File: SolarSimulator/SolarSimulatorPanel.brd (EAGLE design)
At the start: 155 x 77 mm, 82 parts, among them U1 Red Driver, U2 Green Driver, U3 Blue Driver, X1 MKDSN1,5/2-5,08

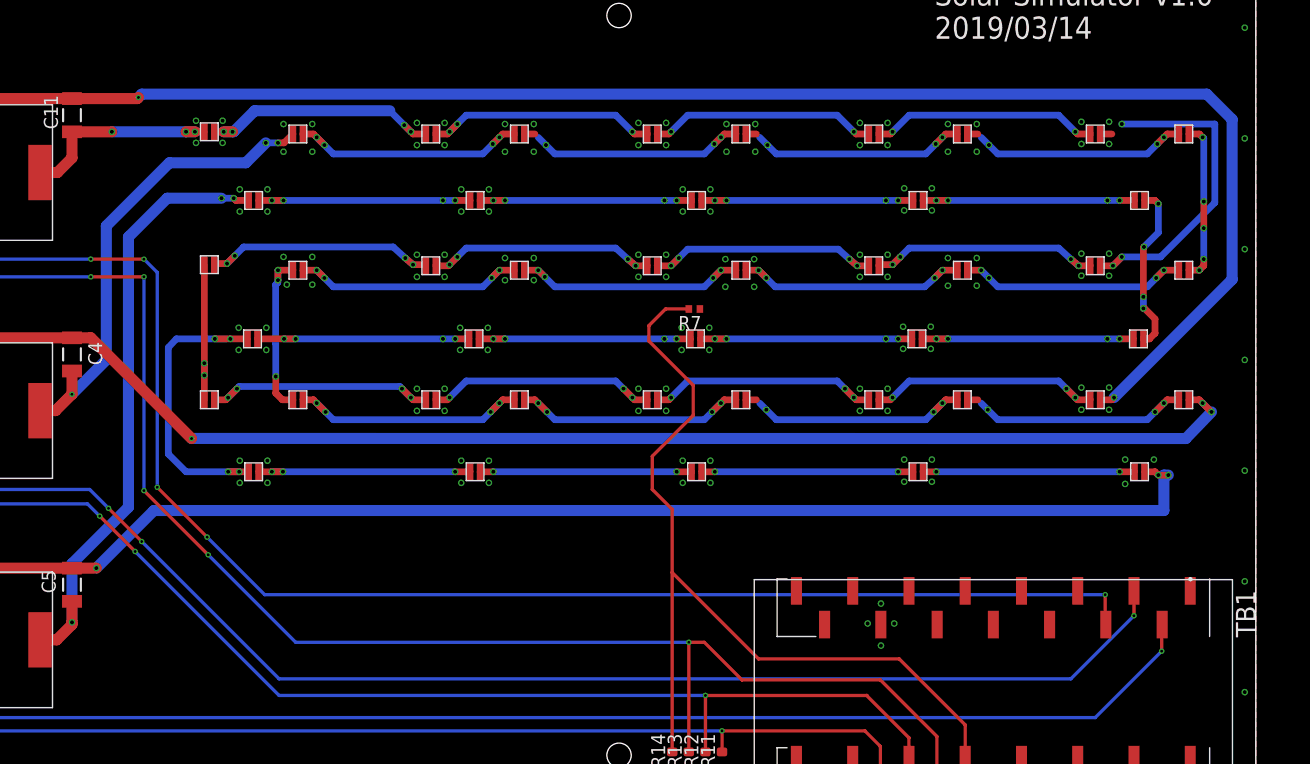
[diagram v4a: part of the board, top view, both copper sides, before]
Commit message: Copper cleanup of solar simulator board. Left LEDs about where they were as much as possible, moved origins ot center on LEDs, tried to sink as much heat to the bottom layer as possible.
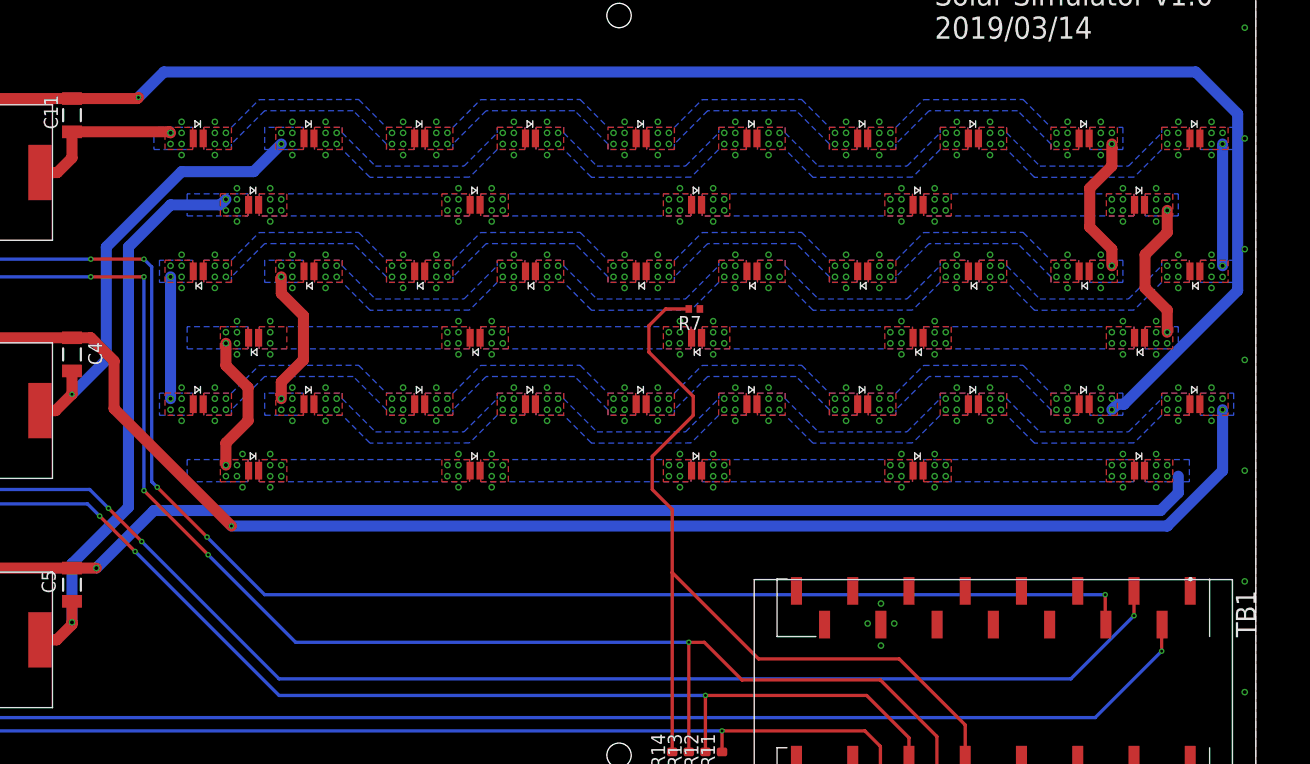
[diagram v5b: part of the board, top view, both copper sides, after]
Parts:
- moved BLUE10 2.28 mm to (59.5, 49.0)
- moved BLUE6 2.22 mm to (139.5, 49.0)
- moved BLUE7 2.22 mm to (119.5, 49.0)
- moved BLUE8 2.22 mm to (99.5, 49.0)
- moved BLUE9 2.22 mm to (79.5, 49.0)
- moved RED14 1.84 mm to (149.5, 37.0)
- moved RED4 1.84 mm to (149.5, 61.0)
- moved RED 1.84 mm to (69.5, 61.0)
- moved RED1 1.84 mm to (89.5, 61.0)
- moved RED10 1.84 mm to (69.5, 37.0)
- moved RED11 1.84 mm to (89.5, 37.0)
- moved RED12 1.84 mm to (109.5, 37.0)
- moved RED13 1.84 mm to (129.5, 37.0)
- moved RED2 1.84 mm to (109.5, 61.0)
- moved RED3 1.84 mm to (129.5, 61.0)
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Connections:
- removed net N$24: BLUE10.INPUT, BLUE9.OUTPUT
- new net N$8SHSHOW: BLUE10.ANODE, BLUE9.CATHODE
- net 88: now also RED4.CATHODE, RED5.ANODE; no longer RED4.OUTPUT, RED5.INPUT
- net BLUE-OUT: now also BLUE1.ANODE; no longer BLUE1.INPUT
- net BLUE-RTN: now also BLUE15.CATHODE; no longer BLUE15.OUTPUT
- net GREEN-RTN: now also GREEN14.CATHODE; no longer GREEN14.OUTPUT
- net GRN-OUT: now also GREEN.ANODE; no longer GREEN.INPUT
- net N$10: now also RED10.CATHODE, RED11.ANODE; no longer RED10.OUTPUT, RED11.INPUT
- net N$11: now also RED11.CATHODE, RED12.ANODE; no longer RED11.OUTPUT, RED12.INPUT
- net N$12: now also RED12.CATHODE, RED13.ANODE; no longer RED12.OUTPUT, RED13.INPUT
- net N$13: now also RED13.CATHODE, RED14.ANODE; no longer RED13.OUTPUT, RED14.INPUT
- net N$14: now also RED.CATHODE, RED1.ANODE; no longer RED.OUTPUT, RED1.INPUT
- net N$15: now also RED1.CATHODE, RED2.ANODE; no longer RED1.OUTPUT, RED2.INPUT
- net N$16: now also RED2.CATHODE, RED3.ANODE; no longer RED2.OUTPUT, RED3.INPUT
- net N$17: now also RED3.CATHODE, RED4.ANODE; no longer RED3.OUTPUT, RED4.INPUT
- net N$2: now also GREEN10.ANODE, GREEN9.CATHODE; no longer GREEN10.INPUT, GREEN9.OUTPUT
- net N$20: now also BLUE6.CATHODE, BLUE7.ANODE; no longer BLUE6.OUTPUT, BLUE7.INPUT
- net N$21: now also BLUE7.CATHODE, BLUE8.ANODE; no longer BLUE7.OUTPUT, BLUE8.INPUT
- net N$23: now also BLUE8.CATHODE, BLUE9.ANODE; no longer BLUE8.OUTPUT, BLUE9.INPUT
- net N$26: now also BLUE11.CATHODE, BLUE12.ANODE; no longer BLUE11.OUTPUT, BLUE12.INPUT
- net N$27: now also BLUE12.CATHODE, BLUE13.ANODE; no longer BLUE12.OUTPUT, BLUE13.INPUT
- net N$29: now also BLUE13.CATHODE, BLUE14.ANODE; no longer BLUE13.OUTPUT, BLUE14.INPUT
- net N$30: now also BLUE14.CATHODE, BLUE15.ANODE; no longer BLUE14.OUTPUT, BLUE15.INPUT
- net N$31: now also BLUE1.CATHODE, BLUE2.ANODE; no longer BLUE1.OUTPUT, BLUE2.INPUT
- net N$35: now also GREEN.CATHODE, GREEN1.ANODE; no longer GREEN.OUTPUT, GREEN1.INPUT
- net N$36: now also GREEN1.CATHODE, GREEN2.ANODE; no longer GREEN1.OUTPUT, GREEN2.INPUT
- net N$37: now also GREEN2.CATHODE, GREEN3.ANODE; no longer GREEN2.OUTPUT, GREEN3.INPUT
- net N$38: now also GREEN3.CATHODE, GREEN4.ANODE; no longer GREEN3.OUTPUT, GREEN4.INPUT
- net N$39: now also GREEN5.CATHODE, GREEN6.ANODE; no longer GREEN5.OUTPUT, GREEN6.INPUT
- net N$40: now also GREEN6.CATHODE, GREEN7.ANODE; no longer GREEN6.OUTPUT, GREEN7.INPUT
- net N$41: now also GREEN7.CATHODE, GREEN8.ANODE; no longer GREEN7.OUTPUT, GREEN8.INPUT
- net N$42: now also GREEN8.CATHODE, GREEN9.ANODE; no longer GREEN8.OUTPUT, GREEN9.INPUT
- net N$43: now also GREEN10.CATHODE, GREEN11.ANODE; no longer GREEN10.OUTPUT, GREEN11.INPUT
- net N$44: now also GREEN11.CATHODE, GREEN12.ANODE; no longer GREEN11.OUTPUT, GREEN12.INPUT
- net N$45: now also GREEN12.CATHODE, GREEN13.ANODE; no longer GREEN12.OUTPUT, GREEN13.INPUT
- net N$46: now also GREEN13.CATHODE, GREEN14.ANODE; no longer GREEN13.OUTPUT, GREEN14.INPUT
- net N$48: now also BLUE2.CATHODE, BLUE3.ANODE; no longer BLUE2.OUTPUT, BLUE3.INPUT
- net N$49: now also BLUE3.CATHODE, BLUE4.ANODE; no longer BLUE3.OUTPUT, BLUE4.INPUT
- net N$5: now also RED5.CATHODE, RED6.ANODE; no longer RED5.OUTPUT, RED6.INPUT
- net N$50: now also BLUE4.CATHODE, BLUE5.ANODE; no longer BLUE4.OUTPUT, BLUE5.INPUT
- net N$56: now also BLUE5.CATHODE, BLUE6.ANODE; no longer BLUE5.OUTPUT, BLUE6.INPUT
- net N$57: now also BLUE10.CATHODE, BLUE11.ANODE; no longer BLUE10.OUTPUT, BLUE11.INPUT
- net N$7: now also RED6.CATHODE, RED7.ANODE; no longer RED6.OUTPUT, RED7.INPUT
- net N$77: now also GREEN4.CATHODE, GREEN5.ANODE; no longer GREEN4.OUTPUT, GREEN5.INPUT
- net N$8: now also RED7.CATHODE, RED8.ANODE; no longer RED7.OUTPUT, RED8.INPUT
- net N$88: now also RED10.ANODE, RED9.CATHODE; no longer RED10.INPUT, RED9.OUTPUT
- net N$9: now also RED8.CATHODE, RED9.ANODE; no longer RED8.OUTPUT, RED9.INPUT
- net RED-OUT: now also RED.ANODE; no longer RED.INPUT
- net RED-RTN: now also RED14.CATHODE; no longer RED14.OUTPUT
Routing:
- net N$11: track 22.9 -> 0.00 mm, vias 4 -> 8
- net N$10: track 22.9 -> 0.00 mm, vias 4 -> 8
- net N$14: track 22.4 -> 0.00 mm, vias 4 -> 8
- net N$31: track 22.4 -> 0.00 mm, vias 4 -> 8
- net N$26: track 22.4 -> 0.00 mm, vias 4 -> 8
- net N$24: track 22.3 -> 0.00 mm, vias 4 -> 0
- net N$9: track 22.3 -> 0.00 mm, vias 4 -> 8
- net N$7: track 22.3 -> 0.00 mm, vias 4 -> 7
- net N$23: track 22.3 -> 0.00 mm, vias 4 -> 8
- net N$20: track 22.3 -> 0.00 mm, vias 4 -> 8
- net N$21: track 22.2 -> 0.00 mm, vias 4 -> 8
- net N$8: track 22.2 -> 0.00 mm, vias 4 -> 8
- net N$30: track 21.6 -> 0.00 mm, vias 3 -> 8
- net N$29: track 21.6 -> 0.00 mm, vias 3 -> 8
- net N$27: track 21.6 -> 0.00 mm, vias 3 -> 8
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- added copper zone on layer 1, net 88
- added copper zone on layer 16, net 88
- added copper zone on layer 1, net BLUE-OUT
- added copper zone on layer 16, net BLUE-OUT
- added copper zone on layer 1, net BLUE-RTN
- added copper zone on layer 16, net BLUE-RTN
- added copper zone on layer 1, net GREEN-RTN
- added copper zone on layer 16, net GREEN-RTN
- added copper zone on layer 1, net GRN-OUT
- added copper zone on layer 16, net GRN-OUT
- added copper zone on layer 1, net N$10
- added copper zone on layer 16, net N$10
- added copper zone on layer 1, net N$11
- added copper zone on layer 16, net N$11
- added copper zone on layer 1, net N$12
- added copper zone on layer 16, net N$12
- added copper zone on layer 1, net N$13
- added copper zone on layer 16, net N$13
- added copper zone on layer 1, net N$14
- added copper zone on layer 16, net N$14
- added copper zone on layer 1, net N$15
- added copper zone on layer 16, net N$15
- added copper zone on layer 1, net N$16
- added copper zone on layer 16, net N$16
- added copper zone on layer 1, net N$17
- added copper zone on layer 16, net N$17
- added copper zone on layer 1, net N$2
- added copper zone on layer 16, net N$2
- added copper zone on layer 1, net N$20
- added copper zone on layer 16, net N$20
- added copper zone on layer 1, net N$21
- added copper zone on layer 16, net N$21
- added copper zone on layer 1, net N$23
- added copper zone on layer 16, net N$23
- added copper zone on layer 1, net N$26
- added copper zone on layer 16, net N$26
- added copper zone on layer 1, net N$27
- added copper zone on layer 16, net N$27
- added copper zone on layer 1, net N$29
- added copper zone on layer 16, net N$29
- added copper zone on layer 1, net N$30
- added copper zone on layer 16, net N$30
- added copper zone on layer 1, net N$31
- added copper zone on layer 16, net N$31
- added copper zone on layer 1, net N$35
- added copper zone on layer 16, net N$35
- added copper zone on layer 1, net N$36
- added copper zone on layer 16, net N$36
- added copper zone on layer 1, net N$37
- added copper zone on layer 16, net N$37
- added copper zone on layer 1, net N$38
- added copper zone on layer 16, net N$38
- added copper zone on layer 1, net N$39
- added copper zone on layer 16, net N$39
- added copper zone on layer 1, net N$40
- added copper zone on layer 16, net N$40
- added copper zone on layer 1, net N$41
- added copper zone on layer 16, net N$41
- added copper zone on layer 1, net N$42
- added copper zone on layer 16, net N$42
- added copper zone on layer 1, net N$43
- added copper zone on layer 16, net N$43
- added copper zone on layer 1, net N$44
- added copper zone on layer 16, net N$44
- added copper zone on layer 1, net N$45
- added copper zone on layer 16, net N$45
- added copper zone on layer 1, net N$46
- added copper zone on layer 16, net N$46
- added copper zone on layer 1, net N$48
- added copper zone on layer 16, net N$48
- added copper zone on layer 1, net N$49
- added copper zone on layer 16, net N$49
- added copper zone on layer 1, net N$5
- added copper zone on layer 16, net N$5
- added copper zone on layer 1, net N$50
- added copper zone on layer 16, net N$50
- added copper zone on layer 1, net N$56
- added copper zone on layer 16, net N$56
- added copper zone on layer 1, net N$57
- added copper zone on layer 16, net N$57
- added copper zone on layer 1, net N$7
- added copper zone on layer 16, net N$7
- added copper zone on layer 1, net N$77
- added copper zone on layer 16, net N$77
- added copper zone on layer 1, net N$8
- added copper zone on layer 16, net N$8
- added copper zone on layer 1, net N$88
- added copper zone on layer 16, net N$88
- added copper zone on layer 1, net N$8SHSHOW
- added copper zone on layer 16, net N$8SHSHOW
- added copper zone on layer 1, net N$9
- added copper zone on layer 16, net N$9
- added copper zone on layer 1, net RED-OUT
- added copper zone on layer 16, net RED-OUT
- added copper zone on layer 1, net RED-RTN
- added copper zone on layer 16, net RED-RTN

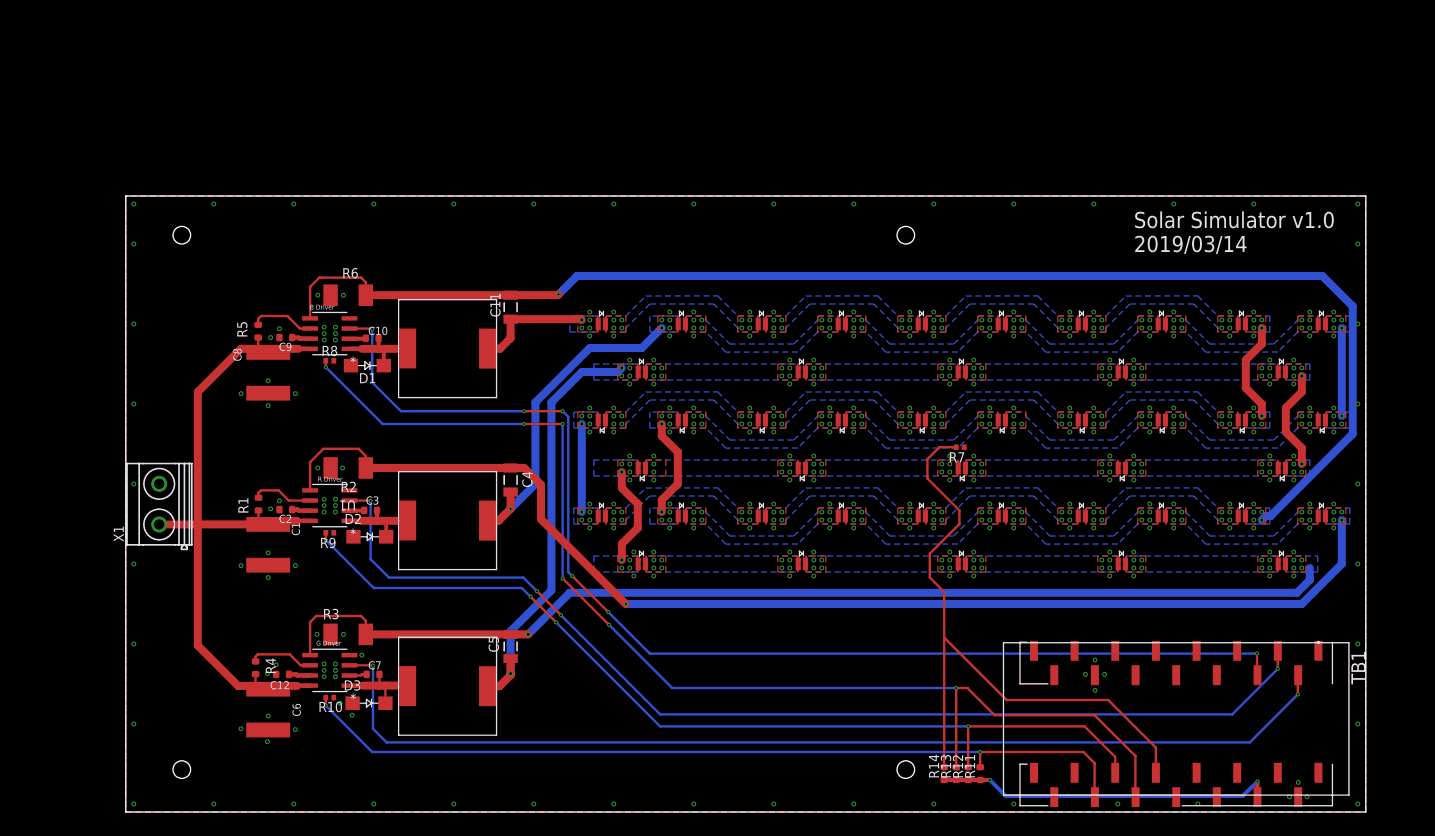
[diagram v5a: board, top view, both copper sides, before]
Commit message: Better ground layout via trace moving, and lots of stitchy.
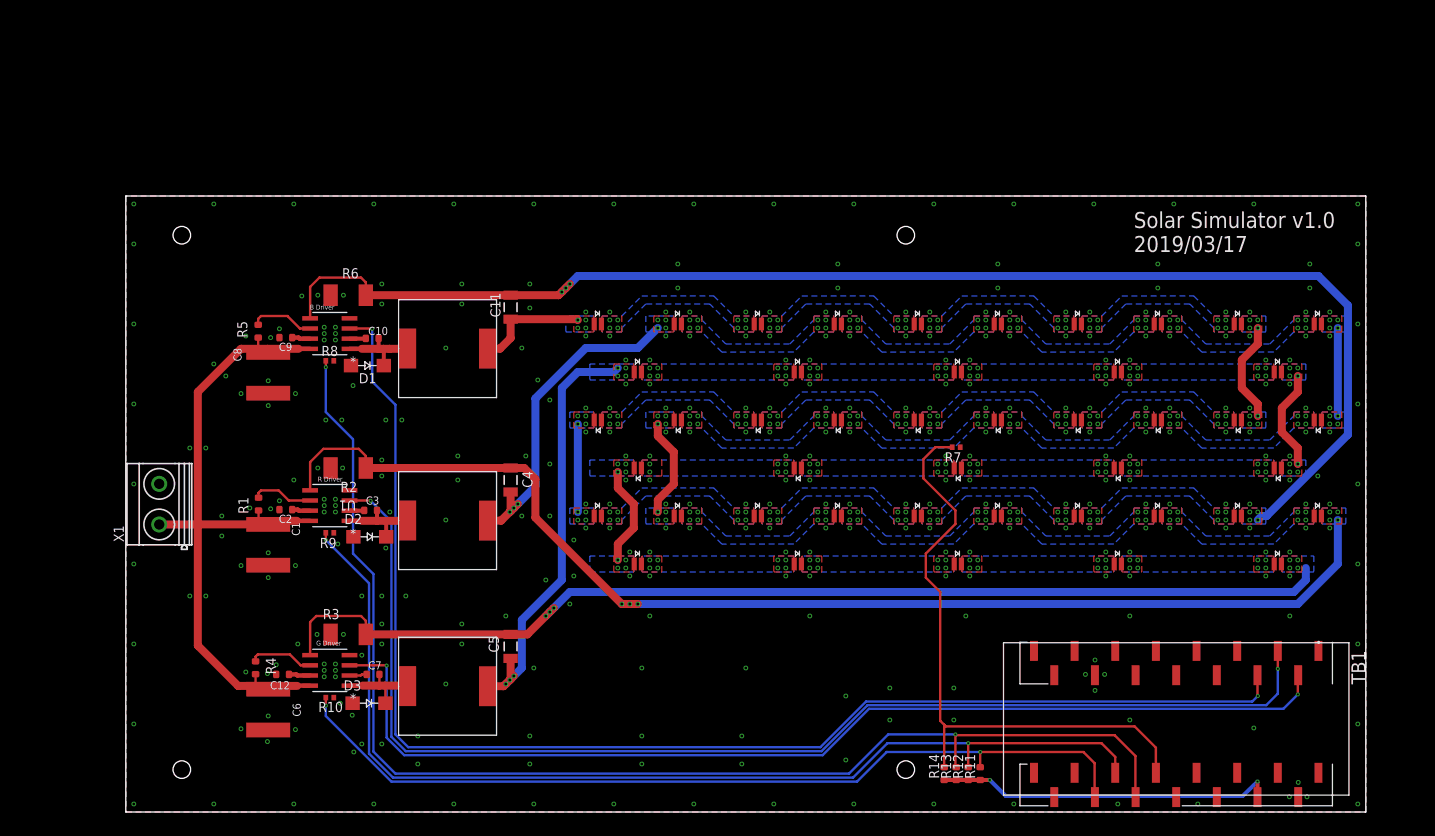
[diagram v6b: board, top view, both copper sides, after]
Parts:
- moved BLUE1 0.50 mm to (59.0, 61.0)
- moved BLUE10 0.50 mm to (59.0, 49.0)
- moved BLUE11 0.50 mm to (59.0, 37.0)
- moved BLUE12 0.50 mm to (79.0, 37.0)
- moved BLUE13 0.50 mm to (99.0, 37.0)
- moved BLUE14 0.50 mm to (119.0, 37.0)
- moved BLUE15 0.50 mm to (139.0, 37.0)
- moved BLUE2 0.50 mm to (79.0, 61.0)
- moved BLUE3 0.50 mm to (99.0, 61.0)
- moved BLUE4 0.50 mm to (119.0, 61.0)
- moved BLUE5 0.50 mm to (139.0, 61.0)
- moved BLUE6 0.50 mm to (139.0, 49.0)
- moved BLUE7 0.50 mm to (119.0, 49.0)
- moved BLUE8 0.50 mm to (99.0, 49.0)
- moved BLUE9 0.50 mm to (79.0, 49.0)
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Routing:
- net PWM_B: track 148.3 -> 168.5 mm, vias 6 -> 2
- net PWM_R: track 136.0 -> 153.1 mm, vias 4 -> 2
- net N$62: track 117.9 -> 131.8 mm, vias 4 -> 2
- net N$61: track 148.5 -> 160.1 mm, vias 6 -> 2
- net N$60: track 82.0 -> 77.6 mm
- net N$91: track 106.2 -> 110.1 mm
- net GRN-OUT: track 52.2 -> 54.5 mm, vias 5 -> 7
- net PWM_G: track 132.1 -> 134.0 mm
- net RED-RTN: track 152.2 -> 154.0 mm, vias 5 -> 7
- net RED-OUT: track 39.8 -> 41.5 mm, vias 5 -> 7
- net BLUE-RTN: track 170.9 -> 171.8 mm, vias 5 -> 7
- net BLUE-OUT: track 14.7 -> 14.2 mm
- net GREEN-RTN: track 135.7 -> 136.0 mm, vias 5 -> 7
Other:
- board text added: "2019/03/17"
- board text removed: "2019/03/14"

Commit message: Big massive shrinkification and OCDification after discussing board with Catie. Moved the Nano off to the overhang area so we could arbitrarily reduce the distance to the solar cell, added two extra holes to get better thermal contact ot the aluminum panel, re-did the DXF, and scrunched everything together.
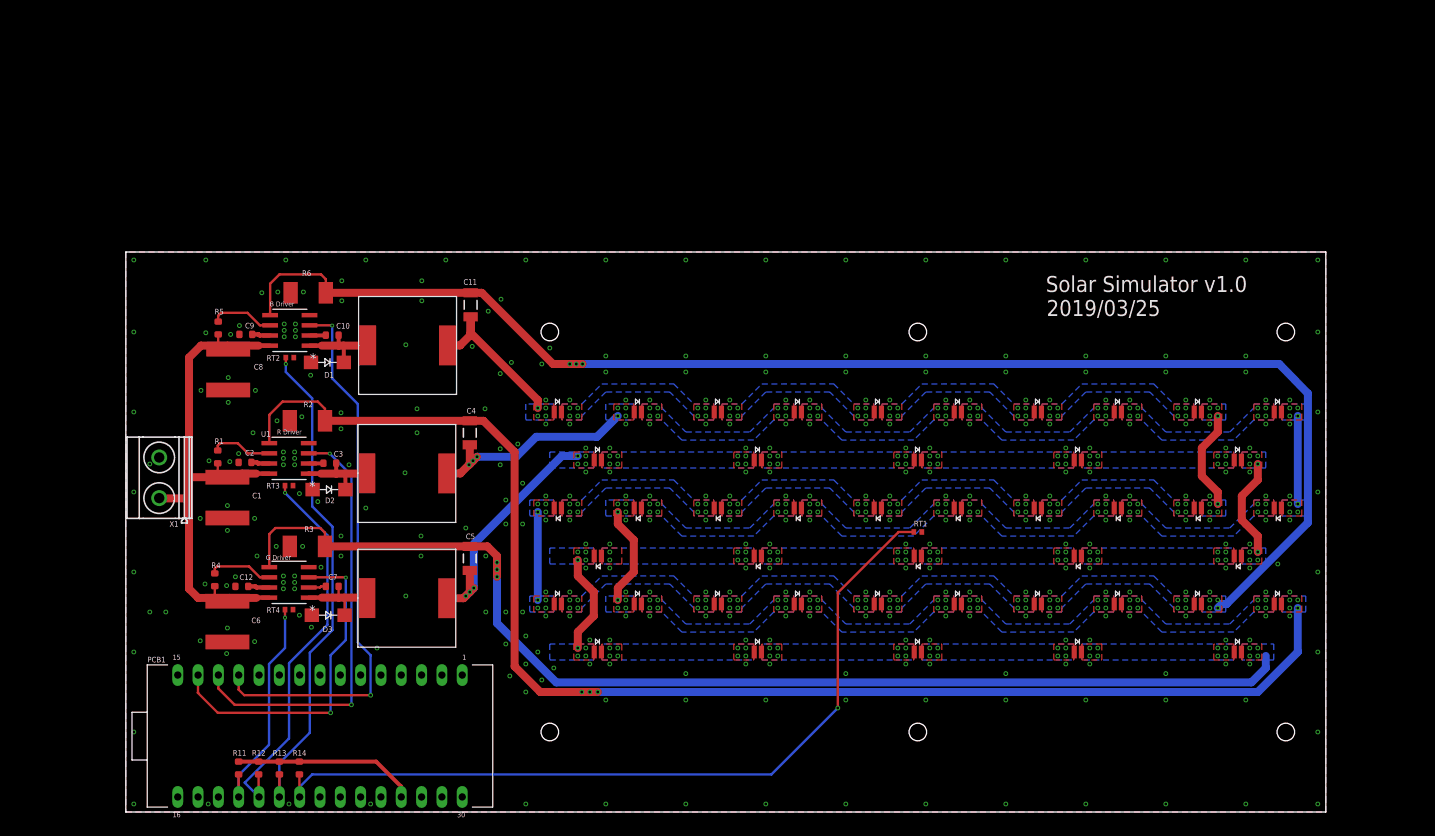
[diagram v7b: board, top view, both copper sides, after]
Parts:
- removed R10, R7, R8, R9: 10K, solarsim:R0402
- removed TB1: ARDUINO_NANO, ARDUINO_NANO:SHIELD_ARDUINO_NANO
- added PCB1: ARDUINO_NANO, ARDUINO_NANO:ARDUINO_NANO_SHIELD
- added RT1, RT2, RT3, RT4: 10K, solarsim:R0402
- U2: value Green Driver -> LM3404HVMA
- moved R11 92.7 mm to (14.1, 5.50), turned to 270 degrees
- moved R12 88.7 mm to (16.6, 5.50), turned to 270 degrees
- moved R13 84.6 mm to (19.2, 5.50), turned to 270 degrees
- moved R14 80.6 mm to (21.7, 5.50), turned to 270 degrees
- moved R3 12.1 mm to (22.7, 33.2)
- moved L3 12.1 mm to (29.0, 20.6)
- moved C12 12.1 mm to (14.5, 28.2)
- moved C5 12.1 mm to (43.0, 31.7)
- moved C6 12.1 mm to (12.7, 23.8)
- moved D3 12.1 mm to (25.3, 24.6)
- moved R4 12.1 mm to (11.1, 29.0)
- moved U2 12.1 mm to (20.4, 28.7)
- moved C7 12.1 mm to (25.8, 28.2)
- moved BLUE1 12.1 mm to (54.0, 50.0)
- moved BLUE10 12.1 mm to (54.0, 38.0)
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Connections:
- removed net N$60: R14.2, R7.2, TB1.52
- removed net N$61: R13.2, R8.2, TB1.51
- removed net N$62: R12.2, R9.2, TB1.50
- removed net N$91: R10.2, R11.2, TB1.49
- removed net PWM_B: TB1.42, U3.3
- removed net PWM_G: TB1.44, U2.3
- removed net PWM_R: TB1.43, U1.3
- new net A0: PCB1.19, R11.2, RT4.2
- new net A1: PCB1.20, R12.2, RT3.2
- new net A2: PCB1.21, R13.2, RT2.2
- new net A3: PCB1.22, R14.2, RT1.2
- new net D10/PWM_R: PCB1.13, U1.3
- new net D11/PWM_G: PCB1.14, U2.3
- new net D9/PWM_B: PCB1.12, U3.3
- new net VIN: PCB1.30
- net +5V: now also PCB1.27; no longer TB1.57
- net 3V3: now also PCB1.17; no longer TB1.47
- net AREF: now also PCB1.18; no longer TB1.48
- net GND: now also PCB1.29, PCB1.4, RT1.1, RT2.1, RT3.1, RT4.1; no longer R10.1, R7.1, R8.1, R9.1, TB1.34, TB1.59
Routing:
- net PWM_B: track 168.5 -> 0.00 mm, vias 2 -> 0
- net N$61: track 160.1 -> 0.00 mm, vias 2 -> 0
- net PWM_R: track 153.1 -> 0.00 mm, vias 2 -> 0
- net PWM_G: track 134.0 -> 0.00 mm, vias 2 -> 0
- net N$62: track 131.8 -> 0.00 mm, vias 2 -> 0
- net N$91: track 110.1 -> 0.00 mm, vias 2 -> 0
- net A3: track 0.00 -> 102.5 mm, vias 0 -> 1
- net N$60: track 77.6 -> 0.00 mm
- net D9/PWM_B: track 0.00 -> 69.7 mm, vias 0 -> 2
- net A2: track 0.00 -> 62.9 mm, vias 0 -> 1
- net D10/PWM_R: track 0.00 -> 54.3 mm, vias 0 -> 2
- net A1: track 0.00 -> 49.0 mm, vias 0 -> 1
- net D11/PWM_G: track 0.00 -> 42.2 mm, vias 0 -> 2
- net A0: track 0.00 -> 28.7 mm, vias 0 -> 1
- net GRN-OUT: track 54.5 -> 31.1 mm
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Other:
- board size 155 x 77 mm -> 150 x 70 mm
- board text added: "2019/03/25"
- board text added: "ALUMINUM"
- board text added: "ARDUINO NANO"
- board text added: "CON"
- board text added: "LEDS"
- board text added: "OVERHANG"
- board text added: "SOLAR SIMULATOR V1.0"
- board text removed: "2019/03/17"
- board text removed: ">NAME"
